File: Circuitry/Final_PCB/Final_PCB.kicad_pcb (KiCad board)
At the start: 2 copper layers, 182.6 x 75.3 mm, 88 parts

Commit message: board revision labelling
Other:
- board text added: "Samuelsen Lab Photologic Experiment Rig REV1"
- board text removed: "Samuelsen Lab Photologic Experiment Rig"
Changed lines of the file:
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@@
     (tags "mounting hole 3.7mm no annular")
     (attr exclude_from_pos_files exclude_from_bom)
-    (fp_text reference "MOUNT" (at 0 -4.7) (layer "F.SilkS")
+    (fp_text reference "MOUNT" (at 0 -3.7) (layer "F.SilkS")
         (effects (font (size 1 1) (thickness 0.15)))
     )
@@
   (gr_line (start 83.7184 142.0508) (end 260.4008 142)
     (stroke (width 0.1) (type default)) (layer "Edge.Cuts"))
-  (gr_text "Samuelsen Lab \nPhotologic Experiment Rig" (at 185.6 135 180) (layer "F.SilkS")
+  (gr_text "Samuelsen Lab \nPhotologic Experiment Rig\nREV1" (at 184.8 132.1 180) (layer "F.SilkS")
     (effects (font (size 2 2) (thickness 0.15)) (justify bottom))
   )

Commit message: final pcb
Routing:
- net /12V_GND: track 298.4 -> 494.6 mm, vias 2 -> 5
- net /5V_ARD1: track 171.9 -> 171.2 mm
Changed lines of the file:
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@@
   (segment (start 104.8 130.26) (end 104.8 130.6) (width 0.25) (layer "B.Cu") (net 1))
   (segment (start 145.625 86.15) (end 147.32 84.455) (width 0.25) (layer "B.Cu") (net 1))
+  (segment (start 209.13 116.51) (end 209.13 122.11) (width 0.25) (layer "F.Cu") (net 2))
   (segment (start 250.745 120.57) (end 250.825 120.65) (width 0.25) (layer "F.Cu") (net 2))
   (segment (start 249.1 92.865) (end 249.1 104.41) (width 0.25) (layer "F.Cu") (net 2))
   (segment (start 223.135 132.47) (end 224.225 131.38) (width 0.25) (layer "F.Cu") (net 2))
   (segment (start 250.825 120.65) (end 250.825 104.14) (width 0.25) (layer "F.Cu") (net 2))
+  (segment (start 226.05 116.51) (end 226.05 121.93) (width 0.25) (layer "F.Cu") (net 2))
+  (segment (start 205.8766 68.5704) (end 206.9 68.5704) (width 0.25) (layer "F.Cu") (net 2))
+  (segment (start 226.0216 101.7052) (end 229.8416 97.8852) (width 0.25) (layer "F.Cu") (net 2))
+  (segment (start 169.722601 128.978847) (end 175.65 123.051448) (width 0.25) (layer "F.Cu") (net 2))
+  (segment (start 175.6774 107.5726) (end 177.85 107.5726) (width 0.25) (layer "F.Cu") (net 2))
   (segment (start 182 107.46) (end 177.9626 107.46) (width 0.25) (layer "F.Cu") (net 2))
   (segment (start 212.42 131.38) (end 213.51 132.47) (width 0.25) (layer "F.Cu") (net 2))
   (segment (start 249.1 104.41) (end 249.08 104.43) (width 0.25) (layer "F.Cu") (net 2))
   (segment (start 189.992 76.253) (end 184.986 76.253) (width 0.25) (layer "F.Cu") (net 2))
+  (segment (start 175.65 123.051448) (end 175.65 107.6) (width 0.25) (layer "F.Cu") (net 2))
+  (segment (start 209.11 101.71) (end 212.92 97.9) (width 0.25) (layer "F.Cu") (net 2))
   (segment (start 230.13 122.13) (end 230.55 121.71) (width 0.25) (layer "F.Cu") (net 2))
   (segment (start 219.45 132.47) (end 223.135 132.47) (width 0.25) (layer "F.Cu") (net 2))
-  (segment (start 204.05 122.13) (end 218.55 122.13) (width 0.25) (layer "F.Cu") (net 2))
+  (segment (start 230.55 116.51) (end 230.55 121.71) (width 0.25) (layer "F.Cu") (net 2))
+  (segment (start 214.21 122.12) (end 214.2 122.13) (width 0.25) (layer "F.Cu") (net 2))
   (segment (start 213.51 132.47) (end 219.45 132.47) (width 0.25) (layer "F.Cu") (net 2))
+  (segment (start 209.11 102.99) (end 209.11 104.19) (width 0.25) (layer "F.Cu") (net 2))
   (segment (start 218.55 122.13) (end 218.55 122.95) (width 0.25) (layer "F.Cu") (net 2))
   (segment (start 197.104 77.343) (end 196.014 76.253) (width 0.25) (layer "F.Cu") (net 2))
+  (segment (start 221.7 122.13) (end 225.85 122.13) (width 0.25) (layer "F.Cu") (net 2))
+  (segment (start 204.05 116.51) (end 204.05 122.13) (width 0.25) (layer "F.Cu") (net 2))
   (segment (start 184.986 76.253) (end 183.896 77.343) (width 0.25) (layer "F.Cu") (net 2))
+  (segment (start 209.15 122.13) (end 214.2 122.13) (width 0.25) (layer "F.Cu") (net 2))
+  (segment (start 225.85 122.13) (end 230.13 122.13) (width 0.25) (layer "F.Cu") (net 2))
   (segment (start 246.54 104.43) (end 249.08 104.43) (width 0.25) (layer "F.Cu") (net 2))
   (segment (start 250.19 91.775) (end 249.1 92.865) (width 0.25) (layer "F.Cu") (net 2))
+  (segment (start 209.11 102.99) (end 209.11 101.71) (width 0.25) (layer "F.Cu") (net 2))
+  (segment (start 226.0216 102.9752) (end 226.0216 101.7052) (width 0.25) (layer "F.Cu") (net 2))
+  (segment (start 214.21 116.51) (end 214.21 122.12) (width 0.25) (layer "F.Cu") (net 2))
+  (segment (start 209.11 104.19) (end 207 106.3) (width 0.25) (layer "F.Cu") (net 2))
+  (segment (start 214.2 122.13) (end 218.55 122.13) (width 0.25) (layer "F.Cu") (net 2))
+  (segment (start 156.63 132.0375) (end 159.688653 128.978847) (width 0.25) (layer "F.Cu") (net 2))
+  (segment (start 159.688653 128.978847) (end 169.722601 128.978847) (width 0.25) (layer "F.Cu") (net 2))
+  (segment (start 221.55 116.51) (end 221.55 121.98) (width 0.25) (layer "F.Cu") (net 2))
   (segment (start 249.08 79.125) (end 246.54 79.125) (width 0.25) (layer "F.Cu") (net 2))
   (segment (start 218.95 131.97) (end 219.45 132.47) (width 0.25) (layer "F.Cu") (net 2))
   (segment (start 177.9626 107.46) (end 177.85 107.5726) (width 0.25) (layer "F.Cu") (net 2))
+  (segment (start 229.8416 97.8852) (end 229.8416 95.466295) (width 0.25) (layer "F.Cu") (net 2))
+  (segment (start 204.05 122.13) (end 209.15 122.13) (width 0.25) (layer "F.Cu") (net 2))
+  (segment (start 175.65 107.6) (end 175.6774 107.5726) (width 0.25) (layer "F.Cu") (net 2))
   (segment (start 218.95 128.25) (end 218.95 131.97) (width 0.25) (layer "F.Cu") (net 2))
   (segment (start 249.1 120.57) (end 250.745 120.57) (width 0.25) (layer "F.Cu") (net 2))
-  (segment (start 218.55 122.13) (end 230.13 122.13) (width 0.25) (layer "F.Cu") (net 2))
   (segment (start 250.535 104.43) (end 249.08 104.43) (width 0.25) (layer "F.Cu") (net 2))
   (segment (start 250.825 104.14) (end 250.535 104.43) (width 0.25) (layer "F.Cu") (net 2))
@@
   (segment (start 249.08 79.125) (end 250.19 80.235) (width 0.25) (layer "F.Cu") (net 2))
   (segment (start 196.014 76.253) (end 189.992 76.253) (width 0.25) (layer "F.Cu") (net 2))
+  (segment (start 226.05 121.93) (end 225.85 122.13) (width 0.25) (layer "F.Cu") (net 2))
+  (segment (start 209.13 122.11) (end 209.15 122.13) (width 0.25) (layer "F.Cu") (net 2))
+  (segment (start 229.8416 95.466295) (end 226.025305 91.65) (width 0.25) (layer "F.Cu") (net 2))
+  (segment (start 197.104 77.343) (end 205.8766 68.5704) (width 0.25) (layer "F.Cu") (net 2))
+  (segment (start 226.025305 91.65) (end 217.8 91.65) (width 0.25) (layer "F.Cu") (net 2))
+  (segment (start 218.55 122.13) (end 221.7 122.13) (width 0.25) (layer "F.Cu") (net 2))
+  (segment (start 221.55 121.98) (end 221.7 122.13) (width 0.25) (layer "F.Cu") (net 2))
   (segment (start 182 84.245) (end 189.992 76.253) (width 0.25) (layer "F.Cu") (net 2))
   (via (at 218.55 122.95) (size 0.8) (drill 0.4) (layers "F.Cu" "B.Cu") (net 2))
+  (via (at 175.6774 107.5726) (size 0.8) (drill 0.4) (layers "F.Cu" "B.Cu") (net 2))
+  (via (at 207 106.3) (size 0.8) (drill 0.4) (layers "F.Cu" "B.Cu") (net 2))
+  (via (at 217.8 91.65) (size 0.8) (drill 0.4) (layers "F.Cu" "B.Cu") (net 2))
   (via (at 218.95 128.25) (size 0.8) (drill 0.4) (layers "F.Cu" "B.Cu") (net 2))
+  (segment (start 175.6774 98.5426) (end 175.6774 107.5726) (width 0.25) (layer "B.Cu") (net 2))
+  (segment (start 218.55 123.45) (end 218.55 127.85) (width 0.25) (layer "B.Cu") (net 2))
+  (segment (start 182 92.22) (end 175.6774 98.5426) (width 0.25) (layer "B.Cu") (net 2))
   (segment (start 187.62 102.38) (end 194.7 102.38) (width 0.25) (layer "B.Cu") (net 2))
   (segment (start 184.92 92.6) (end 184.4 92.6) (width 0.25) (layer "B.Cu") (net 2))
@@
   (segment (start 194.7 102.38) (end 184.92 92.6) (width 0.25) (layer "B.Cu") (net 2))
   (segment (start 106.14 123.16) (end 107.6 121.7) (width 0.25) (layer "B.Cu") (net 2))
+  (segment (start 211.5 68.6) (end 211.45 68.65) (width 0.25) (layer "B.Cu") (net 2))
+  (segment (start 207 106.3) (end 207 110.53) (width 0.25) (layer "B.Cu") (net 2))
+  (segment (start 207 110.53) (end 218.55 122.08) (width 0.25) (layer "B.Cu") (net 2))
   (segment (start 106.14 74.545) (end 106.14 123.29) (width 0.25) (layer "B.Cu") (net 2))
   (segment (start 107.6 121.7) (end 120.34 121.7) (width 0.25) (layer "B.Cu") (net 2))
+  (segment (start 211.3704 68.5704) (end 206.9 68.5704) (width 0.25) (layer "B.Cu") (net 2))
+  (segment (start 211.45 80.396769) (end 211.45 68.65) (width 0.25) (layer "B.Cu") (net 2))
   (segment (start 187.4 102.6) (end 187.62 102.38) (width 0.25) (layer "B.Cu") (net 2))
   (segment (start 184.02 92.22) (end 182 92.22) (width 0.25) (layer "B.Cu") (net 2))
-  (segment (start 218.55 122.95) (end 218.55 127.85) (width 0.25) (layer "B.Cu") (net 2))
+  (segment (start 216.8 68.6) (end 211.5 68.6) (width 0.25) (layer "B.Cu") (net 2))
   (segment (start 121.94 123.3) (end 121.94 74.555) (width 0.25) (layer "B.Cu") (net 2))
+  (segment (start 218.55 122.08) (end 218.55 123.45) (width 0.25) (layer "B.Cu") (net 2))
+  (segment (start 211.45 68.65) (end 211.3704 68.5704) (width 0.25) (layer "B.Cu") (net 2))
   (segment (start 182 107.46) (end 186.86 102.6) (width 0.25) (layer "B.Cu") (net 2))
   (segment (start 218.55 127.85) (end 218.95 128.25) (width 0.25) (layer "B.Cu") (net 2))
-  (segment (start 181.85 107.61) (end 182 107.46) (width 0.25) (layer "B.Cu") (net 2))
+  (segment (start 217.8 86.746769) (end 211.45 80.396769) (width 0.25) (layer "B.Cu") (net 2))
+  (segment (start 218.55 122.95) (end 218.55 123.45) (width 0.25) (layer "B.Cu") (net 2))
   (segment (start 120.34 121.7) (end 121.94 123.3) (width 0.25) (layer "B.Cu") (net 2))
   (segment (start 186.86 102.6) (end 187.4 102.6) (width 0.25) (layer "B.Cu") (net 2))
   (segment (start 184.4 92.6) (end 184.02 92.22) (width 0.25) (layer "B.Cu") (net 2))
+  (segment (start 217.8 91.65) (end 217.8 86.746769) (width 0.25) (layer "B.Cu") (net 2))
   (segment (start 106.14 123.29) (end 106.14 123.16) (width 0.25) (layer "B.Cu") (net 2))
   (segment (start 224.7616 88.9616) (end 224.7616 90.2652) (width 0.25) (layer "F.Cu") (net 3))
@@
   (segment (start 214.21 114.51) (end 230.55 114.51) (width 0.25) (layer "F.Cu") (net 3))
   (segment (start 205.53 87.97) (end 205.86 88.3) (width 0.25) (layer "F.Cu") (net 3))
-  (segment (start 221.5 111.1036) (end 220.9916 110.5952) (width 0.25) (layer "F.Cu") (net 3))
   (segment (start 199.2 85.6) (end 203.16 85.6) (width 0.25) (layer "F.Cu") (net 3))
   (segment (start 204.05 114.51) (end 214.21 114.51) (width 0.25) (layer "F.Cu") (net 3))

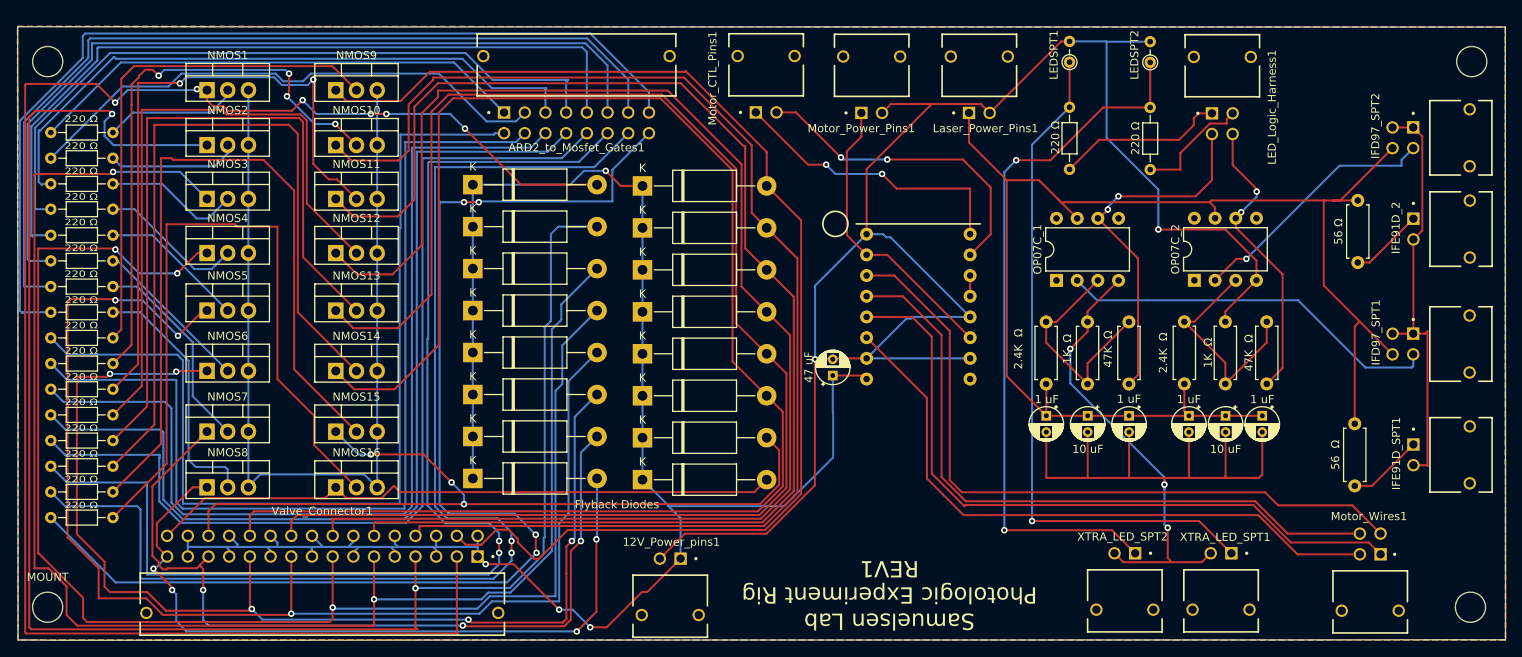
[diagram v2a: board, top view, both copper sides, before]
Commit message: PCB minor correction/revision
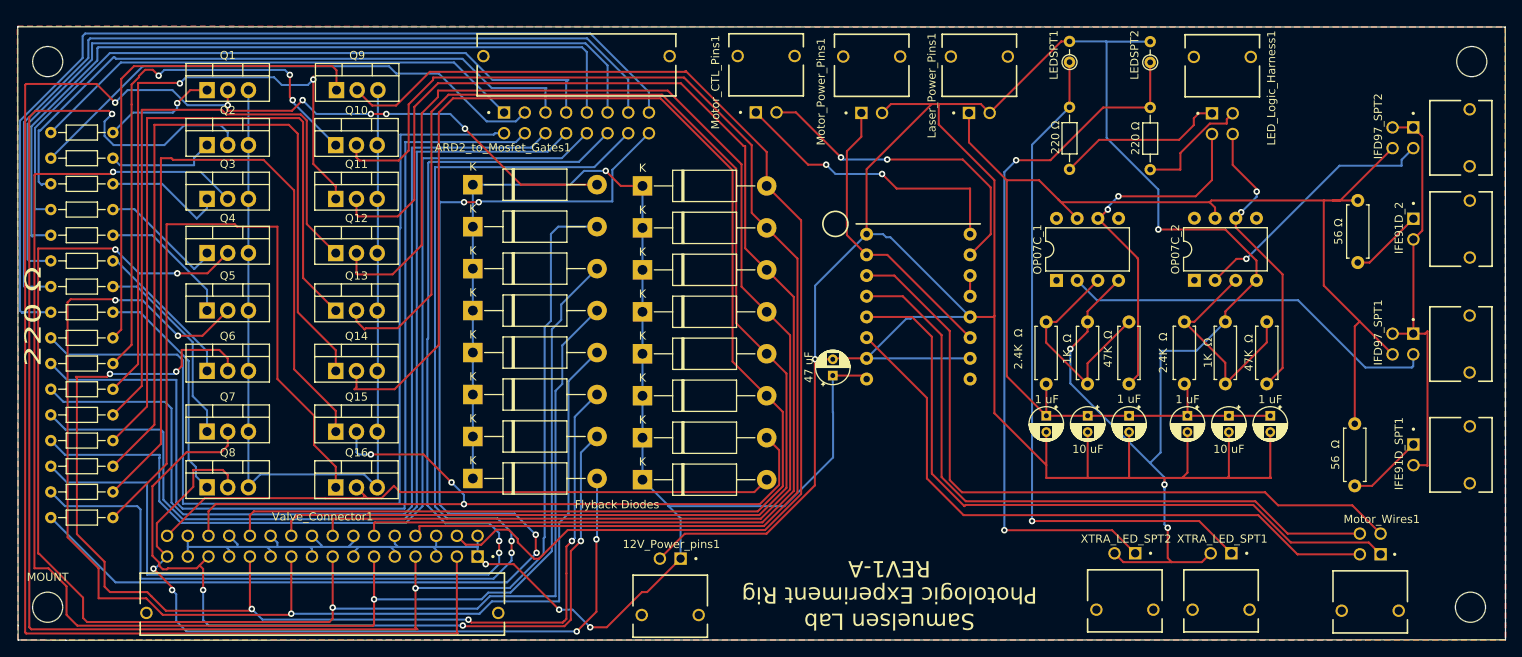
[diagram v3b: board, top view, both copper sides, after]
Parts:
- removed NMOS1, NMOS10, NMOS11, NMOS12, NMOS13, NMOS14, NMOS15, NMOS16, NMOS2, NMOS3, NMOS4, NMOS5, NMOS6, NMOS7, NMOS8, NMOS9: NMOS, Final_PCB_Footprint:TO-220-3_Vertical
- added Q1: Q_NMOS_GDS, Final_PCB_Footprint:TO-220-3_Vertical, F.Cu at (101.1, 74.5)
- added Q10: Q_NMOS_GDS, Final_PCB_Footprint:TO-220-3_Vertical, F.Cu at (116.9, 81.3)
- added Q11: Q_NMOS_GDS, Final_PCB_Footprint:TO-220-3_Vertical, F.Cu at (116.9, 87.9)
- added Q12: Q_NMOS_GDS, Final_PCB_Footprint:TO-220-3_Vertical, F.Cu at (116.9, 94.5)
- added Q13: Q_NMOS_GDS, Final_PCB_Footprint:TO-220-3_Vertical, F.Cu at (116.9, 101.6)
- added Q14: Q_NMOS_GDS, Final_PCB_Footprint:TO-220-3_Vertical, F.Cu at (116.9, 109.0)
- added Q15: Q_NMOS_GDS, Final_PCB_Footprint:TO-220-3_Vertical, F.Cu at (116.9, 116.5)
- added Q16: Q_NMOS_GDS, Final_PCB_Footprint:TO-220-3_Vertical, F.Cu at (116.9, 123.3)
- added Q2: Q_NMOS_GDS, Final_PCB_Footprint:TO-220-3_Vertical, F.Cu at (101.1, 81.3)
- added Q3: Q_NMOS_GDS, Final_PCB_Footprint:TO-220-3_Vertical, F.Cu at (101.1, 87.9)
- added Q4: Q_NMOS_GDS, Final_PCB_Footprint:TO-220-3_Vertical, F.Cu at (101.1, 94.5)
- added Q5: Q_NMOS_GDS, Final_PCB_Footprint:TO-220-3_Vertical, F.Cu at (101.1, 101.6)
- added Q6: Q_NMOS_GDS, Final_PCB_Footprint:TO-220-3_Vertical, F.Cu at (101.1, 109.0)
- added Q7: Q_NMOS_GDS, Final_PCB_Footprint:TO-220-3_Vertical, F.Cu at (101.1, 116.4)
- added Q8: Q_NMOS_GDS, Final_PCB_Footprint:TO-220-3_Vertical, F.Cu at (101.1, 123.3)
- added Q9: Q_NMOS_GDS, Final_PCB_Footprint:TO-220-3_Vertical, F.Cu at (116.9, 74.5)
- moved C4 0.98 mm to (231.5, 114.5)
- moved C5 0.41 mm to (226.5, 114.5)
- moved C6 0.18 mm to (221.4, 114.5)
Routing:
- net /12V_GND: track 494.6 -> 572.7 mm
- net /V6 GND: track 138.2 -> 145.0 mm
- net /V8 GND: track 91.9 -> 98.4 mm
- net /V2 GND: track 209.3 -> 214.8 mm
- net /V7 GND: track 102.9 -> 106.5 mm
- net Net-(Q8-G): track 31.4 -> 28.2 mm
- net Net-(Q10-G): track 70.0 -> 67.2 mm, vias 4 -> 3
- net Net-(Q2-G): track 16.2 -> 13.4 mm
- net Net-(Q1-G): track 16.6 -> 14.1 mm, vias 0 -> 1
- net /V5 GND: track 156.1 -> 158.6 mm
- net /V3 GND: track 187.2 -> 189.8 mm
- net /V4 GND: track 174.5 -> 177.1 mm
- net Net-(Q4-G): track 17.9 -> 15.6 mm
- net /V9 GND: track 151.3 -> 149.1 mm
- net Net-(Q3-G): track 16.8 -> 15.0 mm
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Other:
- board text added: "Samuelsen Lab Photologic Experiment Rig REV1-A"
- board text removed: "Samuelsen Lab Photologic Experiment Rig REV1"

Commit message: Finishing touches PCB
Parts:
- C1, C3, C4, C6: footprint Capacitor_THT:CP_Radial_D4.0mm_P2.00mm -> Capacitor_THT:CP_Radial_D5.0mm_P2.00mm
- C2, C5: footprint Capacitor_THT:CP_Radial_D4.0mm_P2.00mm -> Capacitor_THT:CP_Radial_D10.0mm_P5.00mm
- moved C3 6.46 mm to (197.6, 114.4)
- moved C4 4.74 mm to (236.3, 114.5)
- moved C2 3.31 mm to (205.8, 114.5)
- moved C5 1.65 mm to (228.1, 114.5)
- moved C6 1.53 mm to (219.8, 114.5)
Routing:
- net /12V_GND: track 572.7 -> 539.6 mm, vias 5 -> 6
- net /5V_ARD1: track 171.5 -> 181.7 mm
